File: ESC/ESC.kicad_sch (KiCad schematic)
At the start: 17 parts, among them Q1 BSC028N06LS3, Q2 BSC028N06LS3, SW1 Boot0, SW2 NRST, U1 STM32F411RETx, U2 IRS2101, Y1 16Mhz?

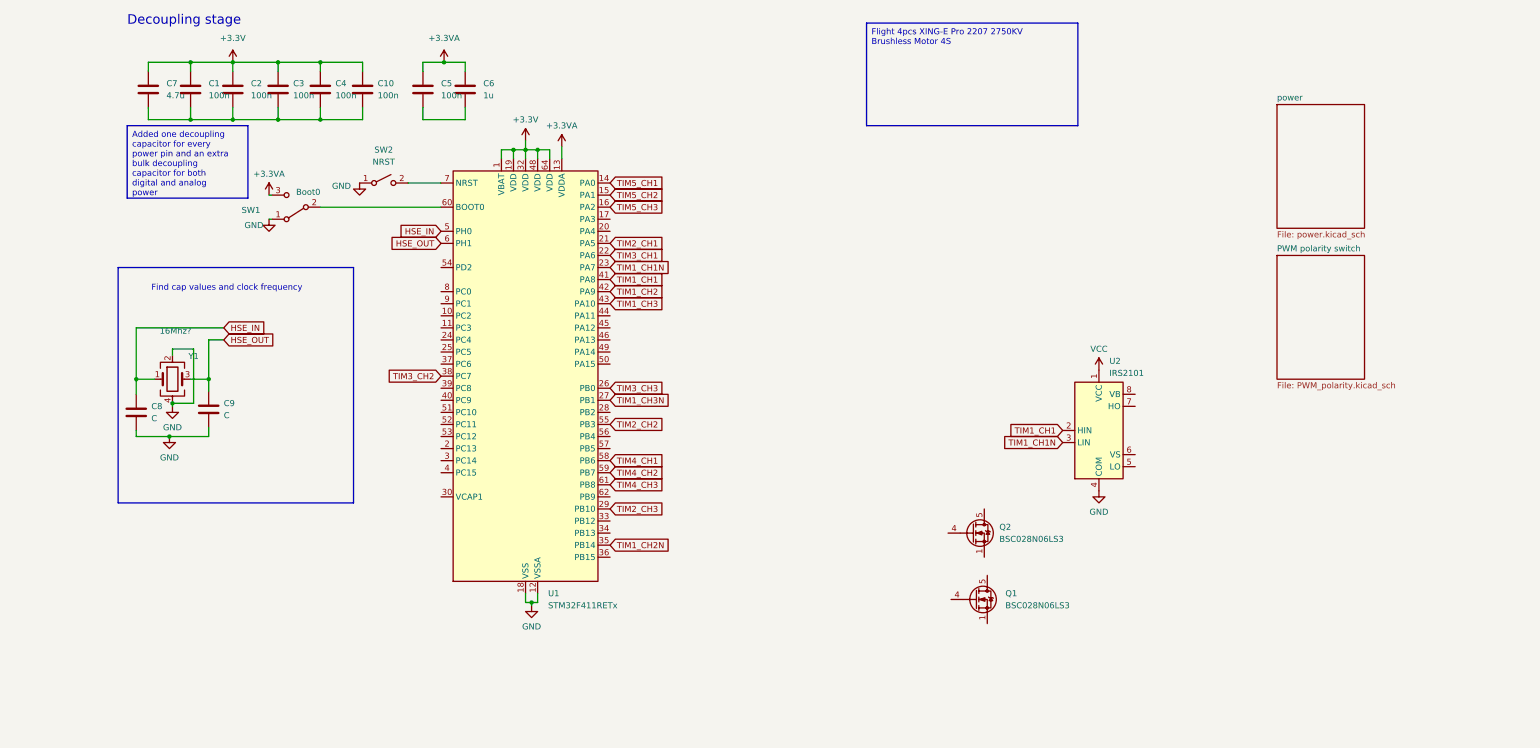
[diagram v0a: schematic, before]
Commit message: added pictures of daq board, updated esc to finish on three phase control
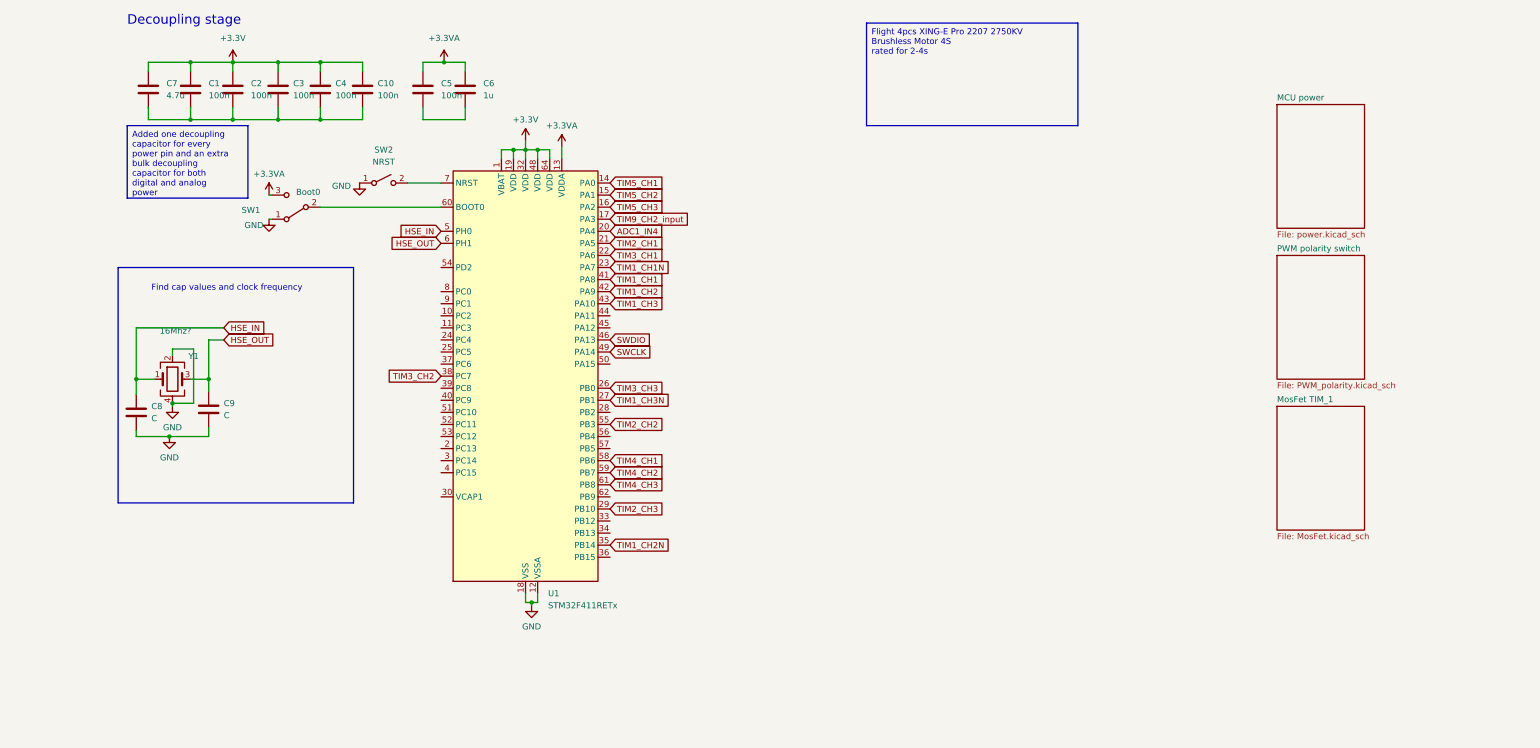
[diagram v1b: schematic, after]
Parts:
- removed Q1, Q2: BSC028N06LS3, Package_TO_SOT_SMD:TDSON-8-1, symbol Transistor_FET:BSC028N06LS3
- removed U2: IRS2101, symbol Driver_FET:IRS2101
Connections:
- net TIM9_CH2_input: now reaches U1.17 (PA3)
- net ADC1_IN4: now reaches U1.20 (PA4)
- net SWDIO: now reaches U1.46 (PA13)
- net SWCLK: now reaches U1.49 (PA14)
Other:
- sheet power renamed MCU power
- added sheet MosFet TIM_1 (MosFet.kicad_sch)
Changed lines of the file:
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@@
     (effects (font (size 1.27 1.27)) (justify left top))
   )
-  (text_box "Flight 4pcs XING-E Pro 2207 2750KV Brushless Motor 4S "
+  (text_box "Flight 4pcs XING-E Pro 2207 2750KV Brushless Motor 4S \nrated for 2-4s"
     (at 170.18 15.24 0) (size 44.45 21.59)
     (stroke (width 0) (type default))
@@
     )
   )
-  (global_label "TIM1_CH1" (shape input) (at 211.455 100.965 180) (fields_autoplaced)
-    (effects (font (size 1.27 1.27) (color 255 0 255 1)) (justify right))
-    (property "Intersheetrefs" "${INTERSHEET_REFS}" (at 199.4589 100.965 0)
-      (effects (font (size 1.27 1.27)) (justify right) hide)
-    )
-  )
   (global_label "TIM4_CH3" (shape input) (at 116.205 112.395 0) (fields_autoplaced)
     (effects (font (size 1.27 1.27) (color 255 255 0 1)) (justify left))
@@
     )
   )
-  (global_label "TIM1_CH1N" (shape input) (at 211.455 103.505 180) (fields_autoplaced)
-    (effects (font (size 1.27 1.27) (color 255 0 255 1)) (justify right))
-    (property "Intersheetrefs" "${INTERSHEET_REFS}" (at 198.1284 103.505 0)
-      (effects (font (size 1.27 1.27)) (justify right) hide)
-    )
-  )
   (global_label "TIM1_CH2" (shape input) (at 116.205 71.755 0) (fields_autoplaced)
     (effects (font (size 1.27 1.27) (color 255 0 255 1)) (justify left))
@@
     (effects (font (size 1.27 1.27) (color 0 255 0 1)) (justify left))
     (property "Intersheetrefs" "${INTERSHEET_REFS}" (at 128.2011 53.975 0)
+      (effects (font (size 1.27 1.27)) (justify left) hide)
+    )
+  )
+  (global_label "SWCLK" (shape input) (at 116.205 84.455 0) (fields_autoplaced)
+    (effects (font (size 1.27 1.27) (color 204 102 0 1)) (justify left))
+    (property "Intersheetrefs" "${INTERSHEET_REFS}" (at 125.4192 84.455 0)
+      (effects (font (size 1.27 1.27)) (justify left) hide)
+    )
+  )
+  (global_label "TIM9_CH2_input" (shape input) (at 116.205 56.515 0) (fields_autoplaced)
+    (effects (font (size 1.27 1.27)) (justify left))
+    (property "Intersheetrefs" "${INTERSHEET_REFS}" (at 133.9462 56.515 0)
       (effects (font (size 1.27 1.27)) (justify left) hide)
     )
@@
     )
   )
+  (global_label "SWDIO" (shape input) (at 116.205 81.915 0) (fields_autoplaced)
+    (effects (font (size 1.27 1.27) (color 204 102 0 1)) (justify left))
+    (property "Intersheetrefs" "${INTERSHEET_REFS}" (at 125.0564 81.915 0)
+      (effects (font (size 1.27 1.27)) (justify left) hide)
+    )
+  )
   (global_label "TIM4_CH2" (shape input) (at 116.205 109.855 0) (fields_autoplaced)
     (effects (font (size 1.27 1.27) (color 255 255 0 1)) (justify left))
@@
     )
   )
+  (global_label "ADC1_IN4" (shape input) (at 116.205 59.055 0) (fields_autoplaced)
+    (effects (font (size 1.27 1.27)) (justify left))
+    (property "Intersheetrefs" "${INTERSHEET_REFS}" (at 128.1407 59.055 0)
+      (effects (font (size 1.27 1.27)) (justify left) hide)
+    )
+  )
   (global_label "TIM1_CH2N" (shape input) (at 116.205 125.095 0) (fields_autoplaced)
     (effects (font (size 1.27 1.27) (color 255 0 255 1)) (justify left))
@@
     )
   )
-  (symbol (lib_id "Transistor_FET:BSC028N06LS3") (at 193.04 136.525 0) (unit 1)
-    (in_bom yes) (on_board yes) (dnp no) (fields_autoplaced)
-    (property "Reference" "Q1" (at 199.39 135.255 0)
-      (effects (font (size 1.27 1.27)) (justify left))
-    )
-    (property "Value" "BSC028N06LS3" (at 199.39 137.795 0)
-      (effects (font (size 1.27 1.27)) (justify left))
-    )
-    (property "Footprint" "Package_TO_SOT_SMD:TDSON-8-1" (at 198.12 138.43 0)
-      (effects (font (size 1.27 1.27) italic) (justify left) hide)
-    )
-    (property "Datasheet" "http://www.infineon.com/dgdl/Infineon-BSC028N06LS3-DS-v02_02-en.pdf?fileId=db3a30431ddc9372011ebafa4c607f8c" (at 193.04 136.525 90)
-      (effects (font (size 1.27 1.27)) (justify left) hide)
-    )
-    (pin "1")
-    (pin "2")
-    (pin "3")
-    (pin "4")
-    (pin "5")
-    (instances
-      (project "ESC"
-        (path "/88e9b63e-ca06-4d41-87b7-50146fa458bf"
-          (reference "Q1") (unit 1)
-        )
-      )
-    )
-  )
-  (symbol (lib_id "Driver_FET:IRS2101") (at 219.075 100.965 0) (unit 1)
-    (in_bom yes) (on_board yes) (dnp no) (fields_autoplaced)
-    (property "Reference" "U2" (at 221.2691 86.36 0)
-      (effects (font (size 1.27 1.27)) (justify left))
-    )
-    (property "Value" "IRS2101" (at 221.2691 88.9 0)
-      (effects (font (size 1.27 1.27)) (justify left))
-    )
-    (property "Footprint" "" (at 219.075 100.965 0)
-      (effects (font (size 1.27 1.27) italic) hide)
-    )
-    (property "Datasheet" "https://www.infineon.com/dgdl/ir2101.pdf?fileId=5546d462533600a4015355c7a755166c" (at 219.075 100.965 0)
-      (effects (font (size 1.27 1.27)) hide)
-    )
-    (pin "1")
-    (pin "2")
-    (pin "3")
-    (pin "4")
-    (pin "5")
-    (pin "6")
-    (pin "7")
-    (pin "8")
-    (instances
-      (project "ESC"
-        (path "/88e9b63e-ca06-4d41-87b7-50146fa458bf"
-          (reference "U2") (unit 1)
-        )
-      )
-    )
-  )
   (symbol (lib_id "Device:C") (at 27.94 29.21 0) (unit 1)
     (in_bom yes) (on_board yes) (dnp no) (fields_autoplaced)
@@
         (path "/88e9b63e-ca06-4d41-87b7-50146fa458bf"
           (reference "#PWR04") (unit 1)
-        )
-      )
-    )
-  )
-  (symbol (lib_id "Transistor_FET:BSC028N06LS3") (at 192.405 122.555 0) (unit 1)
-    (in_bom yes) (on_board yes) (dnp no) (fields_autoplaced)
-    (property "Reference" "Q2" (at 198.12 121.285 0)
-      (effects (font (size 1.27 1.27)) (justify left))
-    )
-    (property "Value" "BSC028N06LS3" (at 198.12 123.825 0)
-      (effects (font (size 1.27 1.27)) (justify left))
-    )
-    (property "Footprint" "Package_TO_SOT_SMD:TDSON-8-1" (at 197.485 124.46 0)
-      (effects (font (size 1.27 1.27) italic) (justify left) hide)
-    )
-    (property "Datasheet" "http://www.infineon.com/dgdl/Infineon-BSC028N06LS3-DS-v02_02-en.pdf?fileId=db3a30431ddc9372011ebafa4c607f8c" (at 192.405 122.555 90)
-      (effects (font (size 1.27 1.27)) (justify left) hide)
-    )
-    (pin "1")
-    (pin "2")
-    (pin "3")
-    (pin "4")
-    (pin "5")
-    (instances
-      (project "ESC"
-        (path "/88e9b63e-ca06-4d41-87b7-50146fa458bf"
-          (reference "Q2") (unit 1)
         )
       )
@@
     )
   )
-  (symbol (lib_id "power:GND") (at 219.075 113.665 0) (unit 1)
-    (in_bom yes) (on_board yes) (dnp no) (fields_autoplaced)
-    (property "Reference" "#PWR020" (at 219.075 120.015 0)
-      (effects (font (size 1.27 1.27)) hide)
-    )
-    (property "Value" "GND" (at 219.075 118.11 0)
-      (effects (font (size 1.27 1.27)))
-    )
-    (property "Footprint" "" (at 219.075 113.665 0)
-      (effects (font (size 1.27 1.27)) hide)
-    )
-    (property "Datasheet" "" (at 219.075 113.665 0)
-      (effects (font (size 1.27 1.27)) hide)
-    )
-    (pin "1")
-    (instances
-      (project "ESC"
-        (path "/88e9b63e-ca06-4d41-87b7-50146fa458bf"
-          (reference "#PWR020") (unit 1)
-        )
-      )
-    )
-  )
   (symbol (lib_id "Switch:SW_SPST") (at 68.58 48.895 0) (unit 1)
     (in_bom yes) (on_board yes) (dnp no) (fields_autoplaced)
@@
         (path "/88e9b63e-ca06-4d41-87b7-50146fa458bf"
           (reference "#PWR03") (unit 1)
-        )
-      )
-    )
-  )
-  (symbol (lib_id "power:VCC") (at 219.075 88.265 0) (unit 1)
-    (in_bom yes) (on_board yes) (dnp no) (fields_autoplaced)
-    (property "Reference" "#PWR019" (at 219.075 92.075 0)
-      (effects (font (size 1.27 1.27)) hide)
-    )
-    (property "Value" "VCC" (at 219.075 83.82 0)
-      (effects (font (size 1.27 1.27)))
-    )
-    (property "Footprint" "" (at 219.075 88.265 0)
-      (effects (font (size 1.27 1.27)) hide)
-    )
-    (property "Datasheet" "" (at 219.075 88.265 0)
-      (effects (font (size 1.27 1.27)) hide)
-    )
-    (pin "1")
-    (instances
-      (project "ESC"
-        (path "/88e9b63e-ca06-4d41-87b7-50146fa458bf"
-          (reference "#PWR019") (unit 1)
         )
       )
@@
     (stroke (width 0.1524) (type solid))
     (fill (color 0 0 0 0.0000))
-    (property "Sheetname" "power" (at 256.54 31.6734 0)
+    (property "Sheetname" "MCU power" (at 256.54 31.6734 0)
       (effects (font (size 1.27 1.27)) (justify left bottom))
     )
@@
       )
     )
+  )
+  (sheet (at 256.54 95.885) (size 18.415 26.035) (fields_autoplaced)
+    (stroke (width 0.1524) (type solid))
+    (fill (color 0 0 0 0.0000))
+    (property "Sheetname" "MosFet TIM_1" (at 256.54 95.1734 0)
+      (effects (font (size 1.27 1.27)) (justify left bottom))
+    )
+    (property "Sheetfile" "MosFet.kicad_sch" (at 256.54 122.5046 0)
+      (effects (font (size 1.27 1.27)) (justify left top))
+    )
+    (instances
+      (project "ESC"
+        (path "/88e9b63e-ca06-4d41-87b7-50146fa458bf" (page "4"))
+      )
+    )

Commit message: finished first mock up of the esc scheamtic still need to check everything works tho
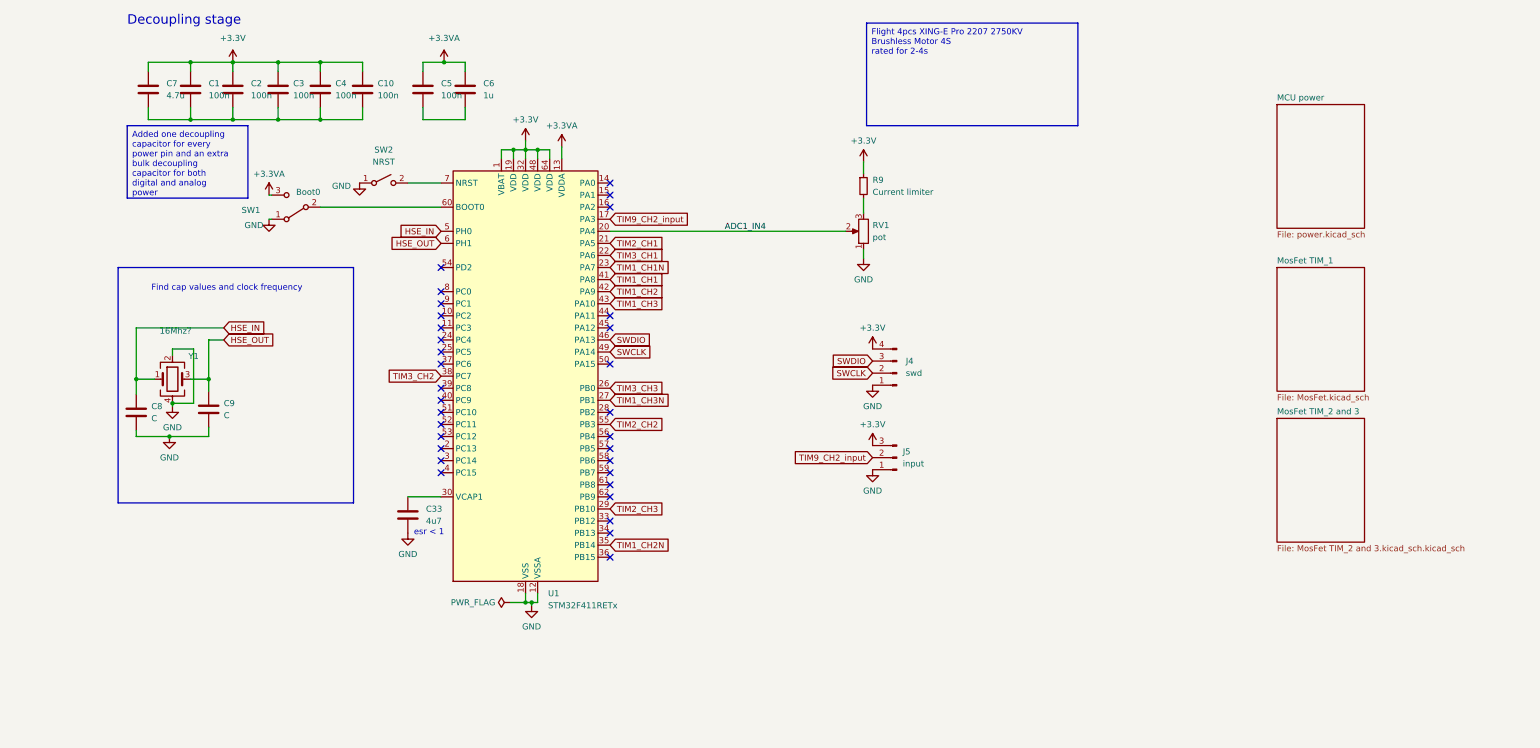
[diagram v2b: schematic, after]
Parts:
- added C33: 4u7, Capacitor_SMD:C_0603_1608Metric_Pad1.08x0.95mm_HandSolder, symbol Device:C
- added J4: swd, symbol Connector:Conn_01x04_Pin
- added J5: input, symbol Connector:Conn_01x03_Pin
- added R9: Current limiter, Resistor_SMD:R_0603_1608Metric_Pad0.98x0.95mm_HandSolder, symbol Device:R_Small
- added RV1: pot, Potentiometer_THT:Potentiometer_Alps_RK09K_Single_Horizontal, symbol Device:R_Potentiometer
- C1, C10, C2, C3, C4, C5, C6, C7, C8, C9: footprint (none) -> Capacitor_SMD:C_0603_1608Metric_Pad1.08x0.95mm_HandSolder
- SW1: footprint (none) -> Button_Switch_SMD:SW_SPDT_PCM12
- SW2: footprint (none) -> Button_Switch_SMD:SW_SPST_PTS645
- Y1: footprint (none) -> Crystal:Crystal_SMD_3225-4Pin_3.2x2.5mm
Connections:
- net +3.3V: now also J4.4 (Pin_4), J5.3 (Pin_3), R9.1
- net ADC1_IN4: now also RV1.2
- net GND: now also C33.2, J4.1 (Pin_1), J5.1 (Pin_1), RV1.1
- net SWCLK: now also J4.2 (Pin_2)
- net SWDIO: now also J4.3 (Pin_3)
- net TIM9_CH2_input: now also J5.2 (Pin_2)
- net at U1.30 (VCAP1): now also C33.1
- net TIM4_CH1: no longer names the net of U1.58 (PB6)
- net TIM4_CH2: no longer names the net of U1.59 (PB7)
- net TIM4_CH3: no longer names the net of U1.61 (PB8)
- net TIM5_CH1: no longer names the net of U1.14 (PA0)
- net TIM5_CH2: no longer names the net of U1.15 (PA1)
- net TIM5_CH3: no longer names the net of U1.16 (PA2)
- new net: R9.2, RV1.3
- no-connect marks 0 -> 32
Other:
- removed sheet PWM polarity switch
- added sheet MosFet TIM_2 and 3 (MosFet TIM_2 and 3.kicad_sch.kicad_sch)
- note added: "esr < 1"
